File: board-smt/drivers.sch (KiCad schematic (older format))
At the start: 85 parts, among them Q201 Dual_NMOS, Q202 Dual_NMOS, Q203 Dual_NMOS, Q204 Dual_NMOS, Q205 Dual_NMOS, Q206 Dual_NMOS, Q209 Dual_NMOS, Q210 Dual_NMOS, Q211 Dual_NMOS, Q213 Dual_NMOS, Q214 Dual_NMOS, Q215 Dual_NMOS, Q218 Dual_NMOS, Q219 Dual_NMOS, Q220 Dual_NMOS, Q222 Dual_NMOS, Q223 Dual_NMOS, Q224 Dual_NMOS, Q228 Dual_NMOS, Q229 Dual_NMOS, Q232 Dual_NMOS, Q233 Dual_NMOS, Q235 Dual_NMOS, Q236 Dual_NMOS, Q239 Dual_NMOS, Q240 Dual_NMOS, Q244 Dual_NMOS, Q245 Dual_NMOS, Q247 Dual_NMOS, Q248 Dual_NMOS, Q251 Dual_NMOS, Q252 Dual_NMOS, Q254 Dual_NMOS, Q255 Dual_NMOS, Q256 Dual_NMOS, Q257 Dual_NMOS, Q258 Dual_NMOS, Q259 Dual_NMOS, Q261 Dual_NMOS

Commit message: Added board-prototype.
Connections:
- net RIRQ6: no longer Q256.3 (D)
- net RIRQ7: no longer Q258.3 (D)
- new net RDMGI: Q258.3 (D)
- new net RIAKI: Q256.3 (D)
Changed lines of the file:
@@
 $EndDescr
 $Comp
-L +5V #PWR011
+L +5V #PWR07
 U 1 1 560EF77D
 P 6850 6050
-F 0 "#PWR011" H 6850 5900 50  0001 C CNN
+F 0 "#PWR07" H 6850 5900 50  0001 C CNN
 F 1 "+5V" H 6850 6190 50  0000 C CNN
 F 2 "" H 6850 6050 60  0000 C CNN
@@
 Connection ~ 4350 8700
 $Comp
-L GND #PWR012
+L GND #PWR08
 U 1 1 5611A213
 P 4350 8800
-F 0 "#PWR012" H 4350 8550 50  0001 C CNN
+F 0 "#PWR08" H 4350 8550 50  0001 C CNN
 F 1 "GND" H 4350 8650 50  0000 C CNN
 F 2 "" H 4350 8800 60  0000 C CNN
@@
 	6000 7950 6050 7950
 Text GLabel 8250 6400 2    60   Input ~ 0
-RIRQ6
+RIAKI
 Text GLabel 8250 7650 2    60   Input ~ 0
-RIRQ7
+RDMGI
 Text GLabel 6000 6600 0    60   Input ~ 0
 TIAKO
@@
 BDMGI
 $Comp
-L GND #PWR013
+L GND #PWR09
 U 1 1 56122BE1
 P 6600 3800
-F 0 "#PWR013" H 6600 3550 50  0001 C CNN
+F 0 "#PWR09" H 6600 3550 50  0001 C CNN
 F 1 "GND" H 6600 3650 50  0000 C CNN
 F 2 "" H 6600 3800 60  0000 C CNN
@@
 $EndComp
 $Comp
-L GND #PWR014
+L GND #PWR010
 U 1 1 56124FB9
 P 6700 6800
-F 0 "#PWR014" H 6700 6550 50  0001 C CNN
+F 0 "#PWR010" H 6700 6550 50  0001 C CNN
 F 1 "GND" H 6700 6650 50  0000 C CNN
 F 2 "" H 6700 6800 60  0000 C CNN
@@
 	6950 4000 7050 4000
 $Comp
-L GND #PWR015
+L GND #PWR011
 U 1 1 56126A4E
 P 6950 4400
-F 0 "#PWR015" H 6950 4150 50  0001 C CNN
+F 0 "#PWR011" H 6950 4150 50  0001 C CNN
 F 1 "GND" H 6950 4250 50  0000 C CNN
 F 2 "" H 6950 4400 60  0000 C CNN
@@
 $EndComp
 $Comp
-L GND #PWR016
+L GND #PWR012
 U 1 1 56126C35
 P 6950 5050
-F 0 "#PWR016" H 6950 4800 50  0001 C CNN
+F 0 "#PWR012" H 6950 4800 50  0001 C CNN
 F 1 "GND" H 6950 4900 50  0000 C CNN
 F 2 "" H 6950 5050 60  0000 C CNN
@@
 	1850 1200 1850 7850
 $Comp
-L GND #PWR017
+L GND #PWR013
 U 1 1 5614838D
 P 1850 7850
-F 0 "#PWR017" H 1850 7600 50  0001 C CNN
+F 0 "#PWR013" H 1850 7600 50  0001 C CNN
 F 1 "GND" H 1850 7700 50  0000 C CNN
 F 2 "" H 1850 7850 60  0000 C CNN
@@
 Connection ~ 7800 6600
 $Comp
-L GND #PWR018
+L GND #PWR014
 U 1 1 5614A37B
 P 8150 8050
-F 0 "#PWR018" H 8150 7800 50  0001 C CNN
+F 0 "#PWR014" H 8150 7800 50  0001 C CNN
 F 1 "GND" H 8150 7900 50  0000 C CNN
 F 2 "" H 8150 8050 60  0000 C CNN
@@
 $EndComp
 $Comp
-L GND #PWR019
+L GND #PWR015
 U 1 1 5614A4F1
 P 7800 8200
-F 0 "#PWR019" H 7800 7950 50  0001 C CNN
+F 0 "#PWR015" H 7800 7950 50  0001 C CNN
 F 1 "GND" H 7800 8050 50  0000 C CNN
 F 2 "" H 7800 8200 60  0000 C CNN
@@
 $EndComp
 $Comp
-L GND #PWR020
+L GND #PWR016
 U 1 1 5614A667
 P 8150 6800
-F 0 "#PWR020" H 8150 6550 50  0001 C CNN
+F 0 "#PWR016" H 8150 6550 50  0001 C CNN
 F 1 "GND" H 8150 6650 50  0000 C CNN
 F 2 "" H 8150 6800 60  0000 C CNN
@@
 $EndComp
 $Comp
-L GND #PWR021
+L GND #PWR017
 U 1 1 5614A7DD
 P 6700 8150
-F 0 "#PWR021" H 6700 7900 50  0001 C CNN
+F 0 "#PWR017" H 6700 7900 50  0001 C CNN
 F 1 "GND" H 6700 8000 50  0000 C CNN
 F 2 "" H 6700 8150 60  0000 C CNN
@@
 Connection ~ 6850 7750
 $Comp
-L GND #PWR022
+L GND #PWR018
 U 1 1 5614B927
 P 6850 8100
-F 0 "#PWR022" H 6850 7850 50  0001 C CNN
+F 0 "#PWR018" H 6850 7850 50  0001 C CNN
 F 1 "GND" H 6850 7950 50  0000 C CNN
 F 2 "" H 6850 8100 60  0000 C CNN
@@
 $EndComp
 $Comp
-L GND #PWR023
+L GND #PWR019
 U 1 1 5614BAA9
 P 6850 6750
-F 0 "#PWR023" H 6850 6500 50  0001 C CNN
+F 0 "#PWR019" H 6850 6500 50  0001 C CNN
 F 1 "GND" H 6850 6600 50  0000 C CNN
 F 2 "" H 6850 6750 60  0000 C CNN
@@
 $EndComp
 $Comp
-L GND #PWR024
+L GND #PWR020
 U 1 1 5614BC2B
 P 7800 6950
-F 0 "#PWR024" H 7800 6700 50  0001 C CNN
+F 0 "#PWR020" H 7800 6700 50  0001 C CNN
 F 1 "GND" H 7800 6800 50  0000 C CNN
 F 2 "" H 7800 6950 60  0000 C CNN
@@
 $EndComp
 $Comp
-L +5V #PWR025
+L +5V #PWR021
 U 1 1 5614C580
 P 7800 6250
-F 0 "#PWR025" H 7800 6100 50  0001 C CNN
+F 0 "#PWR021" H 7800 6100 50  0001 C CNN
 F 1 "+5V" H 7800 6390 50  0000 C CNN
 F 2 "" H 7800 6250 60  0000 C CNN
@@
 $EndComp
 $Comp
-L +5V #PWR026
+L +5V #PWR022
 U 1 1 5614C8EF
 P 6850 7400
-F 0 "#PWR026" H 6850 7250 50  0001 C CNN
+F 0 "#PWR022" H 6850 7250 50  0001 C CNN
 F 1 "+5V" H 6850 7540 50  0000 C CNN
 F 2 "" H 6850 7400 60  0000 C CNN
@@
 $EndComp
 $Comp
-L +5V #PWR027
+L +5V #PWR023
 U 1 1 5614CA6E
 P 7800 7500
-F 0 "#PWR027" H 7800 7350 50  0001 C CNN
+F 0 "#PWR023" H 7800 7350 50  0001 C CNN
 F 1 "+5V" H 7800 7640 50  0000 C CNN
 F 2 "" H 7800 7500 60  0000 C CNN

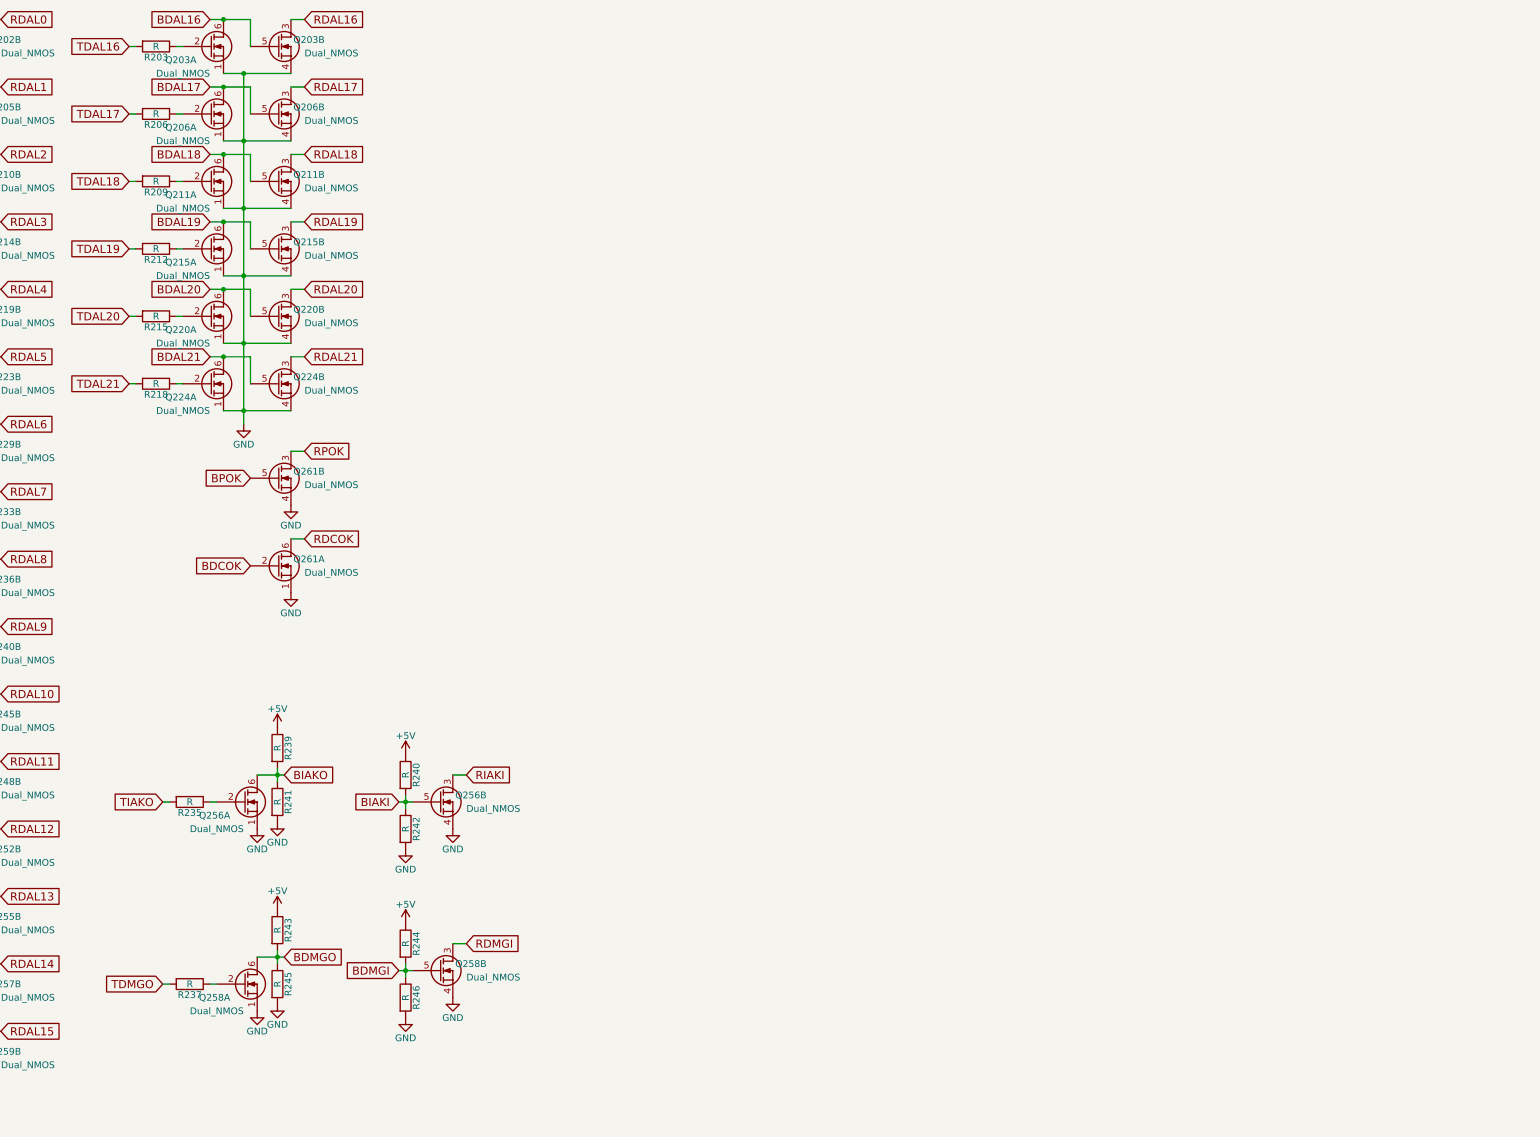
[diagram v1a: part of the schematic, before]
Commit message: Added bus termination.
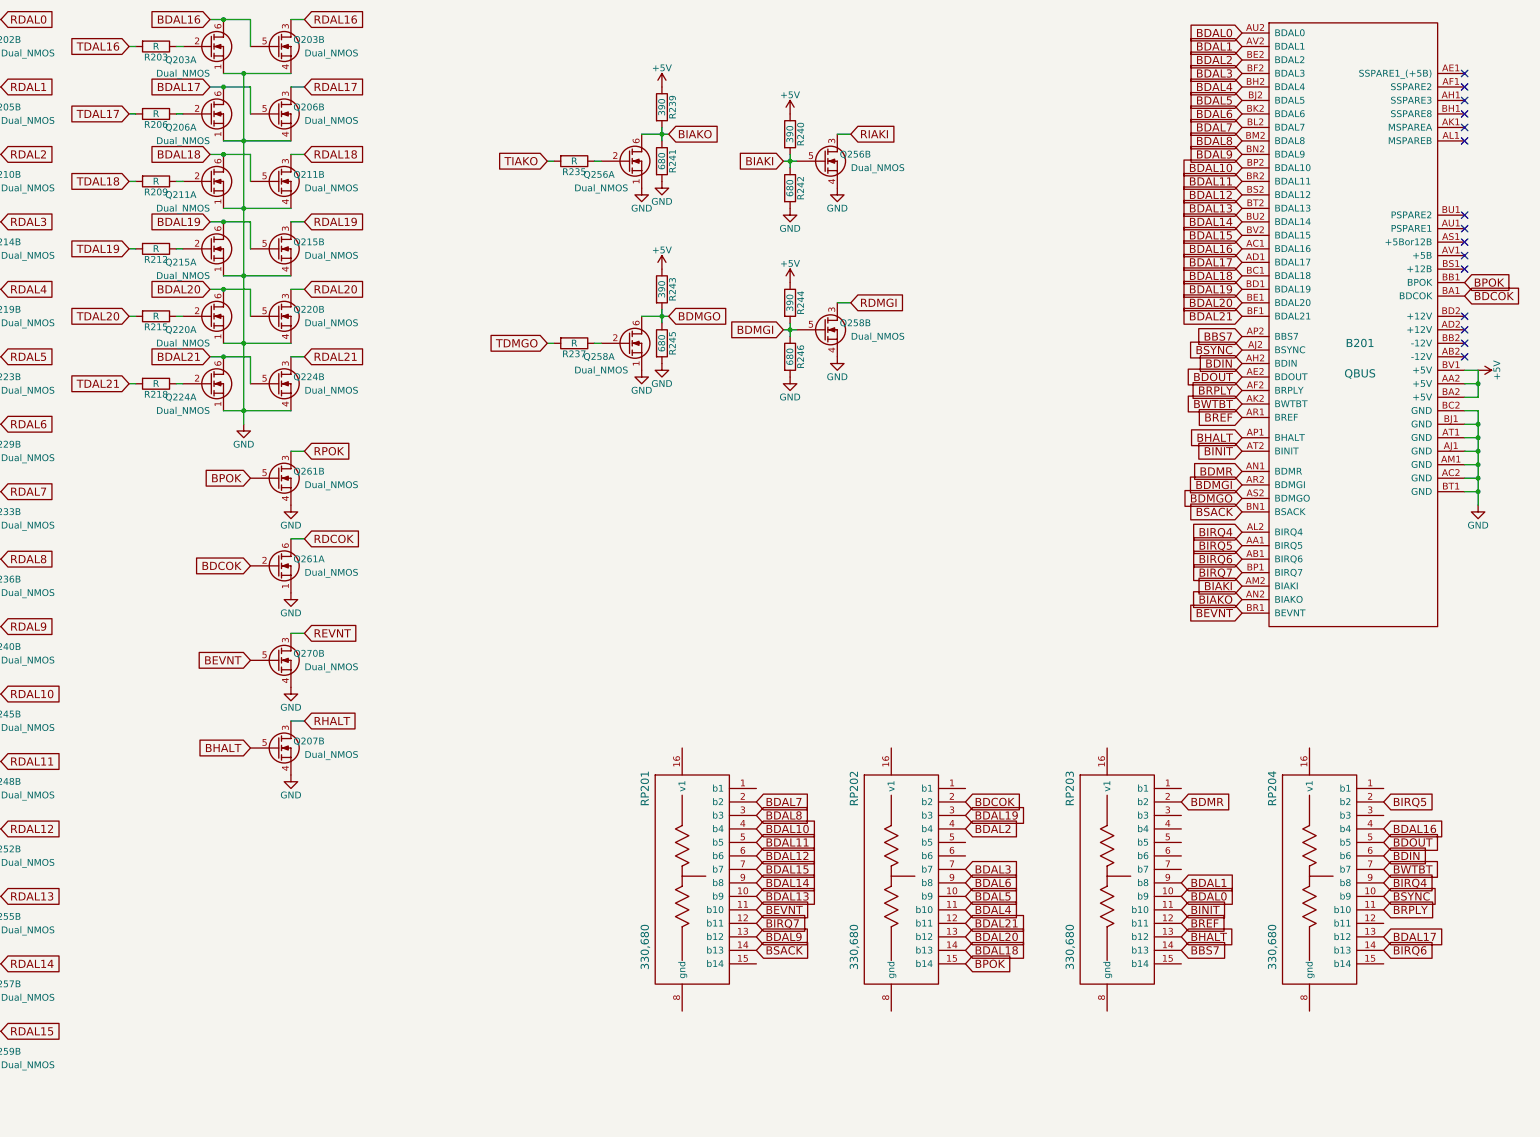
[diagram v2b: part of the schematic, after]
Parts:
- added B201: QBUS, myMods.pretty:Qbus-double, symbol QBUS
- added Q207, Q270: Dual_NMOS, TO_SOT_Packages_SMD:SOT-23-6, symbol Dual_NMOS
- added RP201, RP202, RP203, RP204: 330,680, Housings_SOIC:SOIC-16_3.9x9.9mm_Pitch1.27mm, symbol resistor_pack_-_dual_terminator_14
- R239, R240, R243, R244: value R -> 390
- R241, R242, R245, R246: value R -> 680
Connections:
- net +5V: now also B201.AA2 (+5V), B201.BA2 (+5V), B201.BV1 (+5V)
- net BBS7: now also B201.AP2 (BBS7), RP203.14 (b13)
- net BDAL0: now also B201.AU2 (BDAL0), RP203.10 (b9)
- net BDAL1: now also B201.AV2 (BDAL1), RP203.9 (b8)
- net BDAL10: now also B201.BP2 (BDAL10), RP201.4 (b4)
- net BDAL11: now also B201.BR2 (BDAL11), RP201.5 (b5)
- net BDAL12: now also B201.BS2 (BDAL12), RP201.6 (b6)
- net BDAL13: now also B201.BT2 (BDAL13), RP201.10 (b9)
- net BDAL14: now also B201.BU2 (BDAL14), RP201.9 (b8)
- net BDAL15: now also B201.BV2 (BDAL15), RP201.7 (b7)
- net BDAL16: now also B201.AC1 (BDAL16), RP204.4 (b4)
- net BDAL17: now also B201.AD1 (BDAL17), RP204.13 (b12)
- net BDAL18: now also B201.BC1 (BDAL18), RP202.14 (b13)
- net BDAL19: now also B201.BD1 (BDAL19), RP202.3 (b3)
- net BDAL2: now also B201.BE2 (BDAL2), RP202.4 (b4)
- net BDAL20: now also B201.BE1 (BDAL20), RP202.13 (b12)
- net BDAL21: now also B201.BF1 (BDAL21), RP202.12 (b11)
- net BDAL3: now also B201.BF2 (BDAL3), RP202.7 (b7)
- net BDAL4: now also B201.BH2 (BDAL4), RP202.11 (b10)
- net BDAL5: now also B201.BJ2 (BDAL5), RP202.10 (b9)
- net BDAL6: now also B201.BK2 (BDAL6), RP202.9 (b8)
- net BDAL7: now also B201.BL2 (BDAL7), RP201.2 (b2)
- net BDAL8: now also B201.BM2 (BDAL8), RP201.3 (b3)
- net BDAL9: now also B201.BN2 (BDAL9), RP201.13 (b12)
- net BDCOK: now also B201.BA1 (BDCOK), RP202.2 (b2)
- net BDIN: now also B201.AH2 (BDIN), RP204.6 (b6)
- net BDMGI: now also B201.AR2 (BDMGI)
- net BDMGO: now also B201.AS2 (BDMGO)
- net BDMR: now also B201.AN1 (BDMR), RP203.2 (b2)
- net BDOUT: now also B201.AE2 (BDOUT), RP204.5 (b5)
- net BIAKI: now also B201.AM2 (BIAKI)
- net BIAKO: now also B201.AN2 (BIAKO)
- net BINIT: now also B201.AT2 (BINIT), RP203.11 (b10)
- net BIRQ4: now also B201.AL2 (BIRQ4), RP204.9 (b8)
- net BIRQ5: now also B201.AA1 (BIRQ5), RP204.2 (b2)
- net BIRQ6: now also B201.AB1 (BIRQ6), RP204.14 (b13)
- net BIRQ7: now also B201.BP1 (BIRQ7), RP201.12 (b11)
- net BPOK: now also B201.BB1 (BPOK), RP202.15 (b14)
- net BREF: now also B201.AR1 (BREF), RP203.12 (b11)
- net BRPLY: now also B201.AF2 (BRPLY), RP204.11 (b10)
- net BSACK: now also B201.BN1 (BSACK), RP201.14 (b13)
- net BSYNC: now also B201.AJ2 (BSYNC), RP204.10 (b9)
- net BWTBT: now also B201.AK2 (BWTBT), RP204.7 (b7)
- net GND: now also B201.AC2 (GND), B201.AJ1 (GND), B201.AM1 (GND), B201.AT1 (GND), B201.BC2 (GND), B201.BJ1 (GND), B201.BT1 (GND), Q207.4 (S), Q270.4 (S)
- new net BEVNT: B201.BR1 (BEVNT), Q270.5 (G), RP201.11 (b10)
- new net BHALT: B201.AP1 (BHALT), Q207.5 (G), RP203.13 (b12)
- new net REVNT: Q270.3 (D)
- new net RHALT: Q207.3 (D)
- no-connect marks 0 -> 15
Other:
- moved on the sheet: Q256A, Q256B, Q258A, Q258B, R235, R237, R239, R240, R241, R242, R243, R244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

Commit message: Changed to comparator for bus receivers and rearranged schematic to multiple pages
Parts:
- removed B201: QBUS, myMods.pretty:Qbus-double, symbol QBUS
- removed Q213, Q214, Q215, Q218, Q219, Q220, Q222, Q223, Q224, Q228, Q229, Q232, Q233, Q235, Q236, Q239, Q240, Q244, Q245, Q247, Q248, Q251, Q252, Q254, Q255, Q256, Q257, Q258, Q259, Q261, Q270: Dual_NMOS, TO_SOT_Packages_SMD:SOT-23-6, symbol Dual_NMOS
- removed RP201, RP202, RP203, RP204: 330,680, Housings_SOIC:SOIC-16_3.9x9.9mm_Pitch1.27mm, symbol resistor_pack_-_dual_terminator_14
- added unit 1 of Q207
- added Q208, Q212: Dual_NMOS, TO_SOT_Packages_SMD:SOT-23-6, symbol Dual_NMOS
- added R247, R248, R249, R250, R251, R252, R253, R254, R255, R256, R257, R258, R259, R260, R261, R262, R263, R264, R265, R266, R267, R268, R269, R270, R271, R272: R, Resistors_SMD:R_0603, symbol R
- added U201, U202, U203, U204, U205, U206, U301, U303, U304, U305: CMP401, Housings_SOIC:SOIC-16_3.9x9.9mm_Pitch1.27mm, symbol CMP401
- R201, R202, R203, R204, R205, R206, R207, R208, R209, R210, R211, R212, R213, R214, R215, R216, R217, R218, R219, R220, R221, R222, R223, R224, R225, R226, R227, R228, R229, R230, R231, R232, R233, R234, R235, R236, R237, R238: footprint Resistors_SMD:R_0805 -> Resistors_SMD:R_0603
- R239, R240, R243, R244: value 390 -> R; footprint Resistors_SMD:R_0805 -> Resistors_SMD:R_0603
- R241, R242, R245, R246: value 680 -> R; footprint Resistors_SMD:R_0805 -> Resistors_SMD:R_0603
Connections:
- net BHALT is gone; now on an unnamed net: Q207.5 (G)
- net RDIN is gone; now on net BDAL17: Q209.3 (D)
- net RHALT is gone; now on net BDAL13: Q207.3 (D)
- net RSYNC is gone; now on net BDAL7: Q204.3 (D)
- net TDIN is gone; now on net TDAL6: R207.2
- net TDMGO is gone; now on net TDAL12: R237.2
- net TDMR is gone; now on an unnamed net: R223.2
- net TDOUT is gone; now on net TDAL9: R210.2
- net TIAKO is gone; now on net RDAL10: R235.2
- net TINIT is gone; now on an unnamed net: R221.2
- net TIRQ4 is gone; now on net RDAL2: R227.2
- net TIRQ5 is gone; now on net RDAL4: R229.2
- net TIRQ6 is gone; now on net RDAL6: R231.2
- net TIRQ7 is gone; now on net RDAL8: R233.2
- net TREF is gone; now on an unnamed net: R219.2
- net TRPLY is gone; now on an unnamed net: R213.2
- net TSACK is gone; now on net RDAL0: R225.2
- net TSYNC is gone; now on net TDAL3: R204.2
- net +5V: now also U201.4 (Va+), U202.4 (Va+), U202.4 (Va+), U202.4 (Va+), U202.4 (Va+), U203.4 (Va+), U203.4 (Va+), U203.4 (Va+), U203.4 (Va+), U204.4 (Va+), U204.4 (Va+), U204.4 (Va+), U205.4 (Va+), U205.4 (Va+), U206.4 (Va+), U206.4 (Va+), U206.4 (Va+), U206.4 (Va+), U301.4 (Va+), U301.4 (Va+), U303.4 (Va+), U304.4 (Va+), U305.4 (Va+), U305.4 (Va+); no longer R239.1, R240.1, R243.1, R244.1
- net BBS7: now also Q212.6 (D), U304.10 (-); no longer Q201.5 (G), Q201.6 (D)
- net BDAL0: now also Q201.6 (D), U305.5 (-); no longer Q202.5 (G), Q202.6 (D)
- net BDAL1: now also Q201.3 (D), U305.7 (-); no longer Q205.5 (G), Q205.6 (D)
- net BDAL10: now also Q206.6 (D), U205.5 (-)
- net BDAL11: now also Q206.3 (D), U205.12 (-)
- net BDAL12: now also Q207.6 (D), U206.5 (-)
- net BDAL13: now also U206.7 (-)
- net BDAL14: now also Q208.6 (D), U206.10 (-)
- net BDAL15: now also Q208.3 (D), U206.12 (-)
- net BDAL16: now also Q209.6 (D), U301.5 (-); no longer Q203.5 (G), Q203.6 (D)
- net BDAL17: now also U301.7 (-); no longer Q206.5 (G), Q206.6 (D)
- net BDAL18: now also Q210.6 (D), U201.10 (-); no longer Q211.5 (G), Q211.6 (D)
- net BDAL19: now also Q210.3 (D), U202.12 (-)
- net BDAL2: now also Q202.6 (D), U202.10 (-); no longer Q210.5 (G), Q210.6 (D)
- net BDAL20: now also Q211.6 (D), U202.5 (-)
- net BDAL21: now also Q211.3 (D), U202.7 (-)
- net BDAL3: now also Q202.3 (D), U203.12 (-)
- net BDAL4: now also Q203.6 (D), U203.5 (-)
- net BDAL5: now also Q203.3 (D), U203.7 (-)
- net BDAL6: now also Q204.6 (D), U203.10 (-)
- net BDAL7: now also U204.12 (-)
- net BDAL8: now also Q205.6 (D), U204.5 (-)
- net BDAL9: now also Q205.3 (D), U204.7 (-)
- net BWTBT: now also Q212.3 (D), U303.12 (-)
- net GND: now also Q207.1 (S), Q208.1 (S), Q208.4 (S), Q212.1 (S), Q212.4 (S), U201.13 (Va-), U201.14 (Vd-), U202.13 (Va-), U202.13 (Va-), U202.13 (Va-), U202.13 (Va-), U202.14 (Vd-), U202.14 (Vd-), U202.14 (Vd-), U202.14 (Vd-), U203.13 (Va-), U203.13 (Va-), U203.13 (Va-), U203.13 (Va-), U203.14 (Vd-), U203.14 (Vd-), U203.14 (Vd-), U203.14 (Vd-), U204.13 (Va-), U204.13 (Va-), U204.13 (Va-), U204.14 (Vd-), U204.14 (Vd-), U204.14 (Vd-), U205.13 (Va-), U205.13 (Va-), U205.14 (Vd-), U205.14 (Vd-), U206.13 (Va-), U206.13 (Va-), U206.13 (Va-), U206.13 (Va-), U206.14 (Vd-), U206.14 (Vd-), U206.14 (Vd-), U206.14 (Vd-), U301.13 (Va-), U301.13 (Va-), U301.14 (Vd-), U301.14 (Vd-), U303.13 (Va-), U303.14 (Vd-), U304.13 (Va-), U304.14 (Vd-), U305.13 (Va-), U305.13 (Va-), U305.14 (Vd-), U305.14 (Vd-); no longer R241.2, R242.2, R245.2, R246.2
- net RBS7: now also R271.2, U304.16 (OUT); no longer Q201.3 (D)
- net RDAL0: now also U305.2 (OUT); no longer Q202.3 (D)
- net RDAL1: now also R226.2, U305.1 (OUT); no longer Q205.3 (D)
- net RDAL10: now also U205.2 (OUT)
- net RDAL11: now also R236.2, U205.15 (OUT)
- net RDAL12: now also R261.2, U206.2 (OUT)
- net RDAL13: now also R262.2, U206.1 (OUT)
- net RDAL14: now also R263.2, U206.16 (OUT)
- net RDAL15: now also R264.2, U206.15 (OUT)
- net RDAL16: now also R265.2, U301.2 (OUT); no longer Q203.3 (D)
- net RDAL17: now also R266.2, U301.1 (OUT); no longer Q206.3 (D)
- net RDAL18: now also R267.2, U201.16 (OUT); no longer Q211.3 (D)
- net RDAL19: now also R268.2, U202.15 (OUT)
- net RDAL2: now also U202.16 (OUT); no longer Q210.3 (D)
- net RDAL20: now also R269.2, U202.2 (OUT)
- net RDAL21: now also R270.2, U202.1 (OUT)
- net RDAL3: now also R228.2, U203.15 (OUT)
- net RDAL4: now also U203.2 (OUT)
- net RDAL5: now also R230.2, U203.1 (OUT)
- net RDAL6: now also U203.16 (OUT)
- net RDAL7: now also R232.2, U204.15 (OUT)
- net RDAL8: now also U204.2 (OUT)
- net RDAL9: now also R234.2, U204.1 (OUT)
- net RWTBT: now also R272.2, U303.15 (OUT)
- net TBS7: now also R247.2; no longer R201.2
- net TDAL0: now also R201.2; no longer R202.2
- net TDAL1: now also R202.2; no longer R205.2
- net TDAL10: now also R211.2; no longer R228.2
- net TDAL11: now also R212.2; no longer R230.2
- net TDAL12: no longer R232.2
- net TDAL13: now also R238.2; no longer R234.2
- net TDAL14: now also R239.2; no longer R236.2
- net TDAL15: now also R240.2; no longer R238.2
- net TDAL16: now also R241.2; no longer R203.2
- net TDAL17: now also R242.2; no longer R206.2
- net TDAL18: now also R243.2; no longer R209.2
- net TDAL19: now also R244.2; no longer R212.2
- net TDAL2: now also R203.2; no longer R208.2
- net TDAL20: now also R245.2; no longer R215.2
- net TDAL21: now also R246.2; no longer R218.2
- net TDAL3: no longer R211.2
- net TDAL4: now also R205.2; no longer R214.2
- net TDAL5: now also R206.2; no longer R217.2
- net TDAL6: no longer R220.2
- net TDAL7: now also R208.2; no longer R222.2
- net TDAL8: now also R209.2; no longer R224.2
- net TDAL9: no longer R226.2
- net TWTBT: now also R248.2; no longer R216.2
- net at R204.1: now also Q202.5 (G); no longer Q204.2 (G)
- net at Q209.2 (G): now also R241.1; no longer R207.1
- net at R210.1: now also Q205.5 (G)
- net +1V5: now reaches R213.1
- net +1V5: now also R214.1, R215.1, R216.1, R217.1, R218.1, R219.1, R220.1, R221.1, R222.1, R223.1, R224.1, R249.1, R250.1, R251.1, R252.1, R253.1, R254.1, R255.1, R256.1, R257.1, R258.1, R259.1, R260.1
- net at R225.1: now also U305.6 (+)
- net at R227.1: now also R215.2, U202.9 (+)
- net at R229.1: now also R217.2, U203.6 (+)
- net at R231.1: now also U203.9 (+)
- net at R233.1: now also U204.6 (+)
- net at R202.1: now also Q201.5 (G); no longer Q202.2 (G)
- net at R205.1: now also Q203.2 (G); no longer Q205.2 (G)
- net at Q210.2 (G): now also R243.1; no longer R208.1
- net at R211.1: now also Q206.2 (G)
- net at R226.1: now also R214.2, U305.8 (+)
- net at R228.1: now also R216.2, U203.11 (+)
- net at R230.1: now also R218.2, U203.8 (+)
- net at R232.1: now also R220.2, U204.11 (+)
- net at R234.1: now also R222.2, U204.8 (+)
- net at R236.1: now also R224.2, U205.11 (+)
- net at R203.1: now also Q202.2 (G); no longer Q203.2 (G)
- net at R206.1: now also Q203.5 (G); no longer Q206.2 (G)
- net at Q211.2 (G): now also R245.1; no longer R209.1
- net at R212.1: now also Q206.5 (G)
- net at R235.1: now also U205.6 (+)
- net at R237.1: now also Q207.2 (G)
- net BDIN: no longer names the net of Q209.5 (G)
- net BDIN: now also R242.1; no longer Q209.6 (D)
- net BDMGI: no longer names the net of R246.1
- net BDMGI: now also Q211.5 (G); no longer R244.2
- removed net BDMGO: R243.2, R245.1
- removed net BIAKI: R240.2, R242.1
- removed net BIAKO: R239.2, R241.1
- net BSYNC: no longer names the net of Q204.5 (G)
- net BSYNC: now also R208.1; no longer Q204.6 (D)
- new net: R250.2, R262.1, U206.8 (+)
- new net: R249.2, R261.1, U206.6 (+)
- new net: Q208.5 (G), R240.1
- new net: R252.2, R264.1, U206.11 (+)
- new net: Q208.2 (G), R239.1
- new net: R251.2, R263.1, U206.9 (+)
- new net: R254.2, R266.1, U301.8 (+)
- new net: R253.2, R265.1, U301.6 (+)
- new net: Q210.5 (G), R244.1
- new net: R256.2, R268.1, U202.11 (+)
- new net: R255.2, R267.1, U201.9 (+)
- new net: R258.2, R270.1, U202.8 (+)
- new net: R257.2, R269.1, U202.6 (+)
- new net: Q212.5 (G), R248.1
- new net: R260.2, R272.1, U303.11 (+)
- new net: Q212.2 (G), R247.1
- new net: R259.2, R271.1, U304.9 (+)
- new net: Q204.2 (G), R207.1
- new net: Q205.2 (G), R209.1
- new net +3V3: U201.3 (Vd+), U202.3 (Vd+), U202.3 (Vd+), U202.3 (Vd+), U202.3 (Vd+), U203.3 (Vd+), U203.3 (Vd+), U203.3 (Vd+), U203.3 (Vd+), U204.3 (Vd+), U204.3 (Vd+), U204.3 (Vd+), U205.3 (Vd+), U205.3 (Vd+), U206.3 (Vd+), U206.3 (Vd+), U206.3 (Vd+), U206.3 (Vd+), U301.3 (Vd+), U301.3 (Vd+), U303.3 (Vd+), U304.3 (Vd+), U305.3 (Vd+), U305.3 (Vd+)
- no-connect marks 15 -> 0
